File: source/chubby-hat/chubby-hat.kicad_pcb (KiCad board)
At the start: 2 copper layers, 143.5 x 91.4 mm, 148 parts, among them J1 RP2040.SWD, J10 USB_C_Receptacle_USB2.0, J11 HUB75, J12 HUB75, J13 HUB75, J14 v7.0, J15 v8.0, J16 HUB75, J17 Conn_01x02, J18 HUB75, J19 HUB75, J2 Conn_ARM_JTAG_SWD_10, J20 V7.0, J21 V8.0, J22 HUB75, J23 HUB75, J3 Conn_ARM_JTAG_SWD_10, J4 TC2030, J5 UART, J6 5V, J7 5V, J8 5V, J9 5V, Q1 BC807DS,115, Q2 AO3401A, Q3 BC807DS,115, Q4 AO3401A, SW1 RUN, SW2 BOOT, U1 AMS1117-3.3, U2 RP2040-Zero, U3 USBLC6-2SC6, U4 P25Q40H-SSH-IT, U5 RP2040, Y1 12M

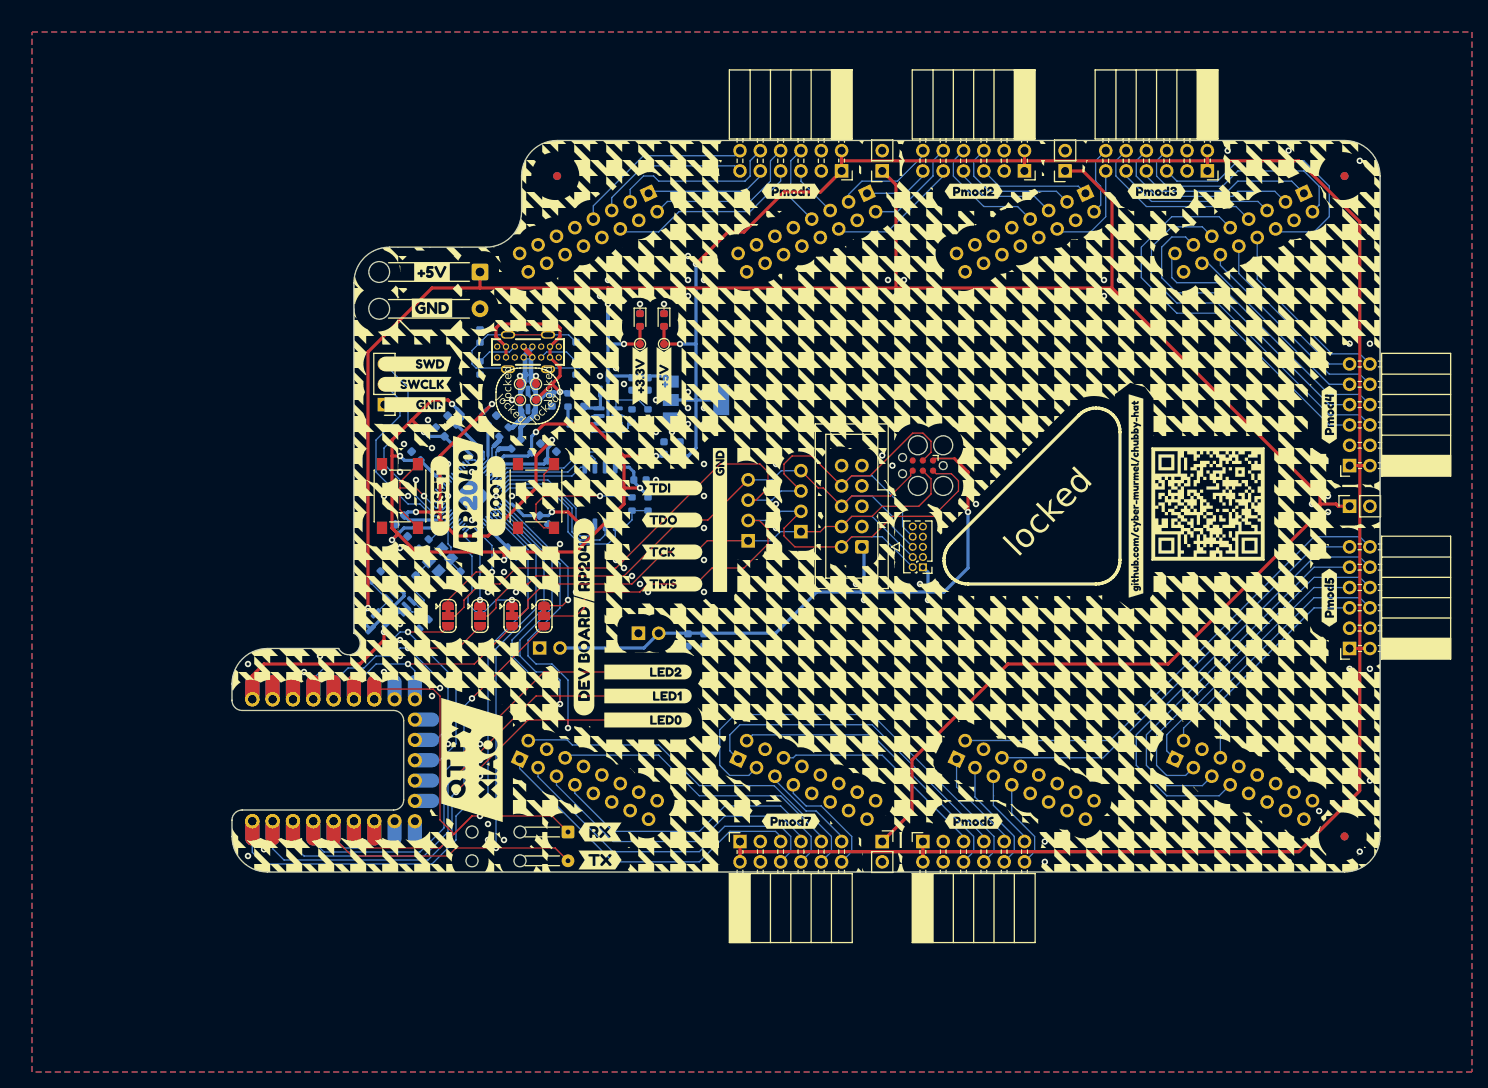
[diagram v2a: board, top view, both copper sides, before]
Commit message: rotated v8 jtag connector - closes #10; moved aux jtag connectors and pmod wires to makes space for #14;
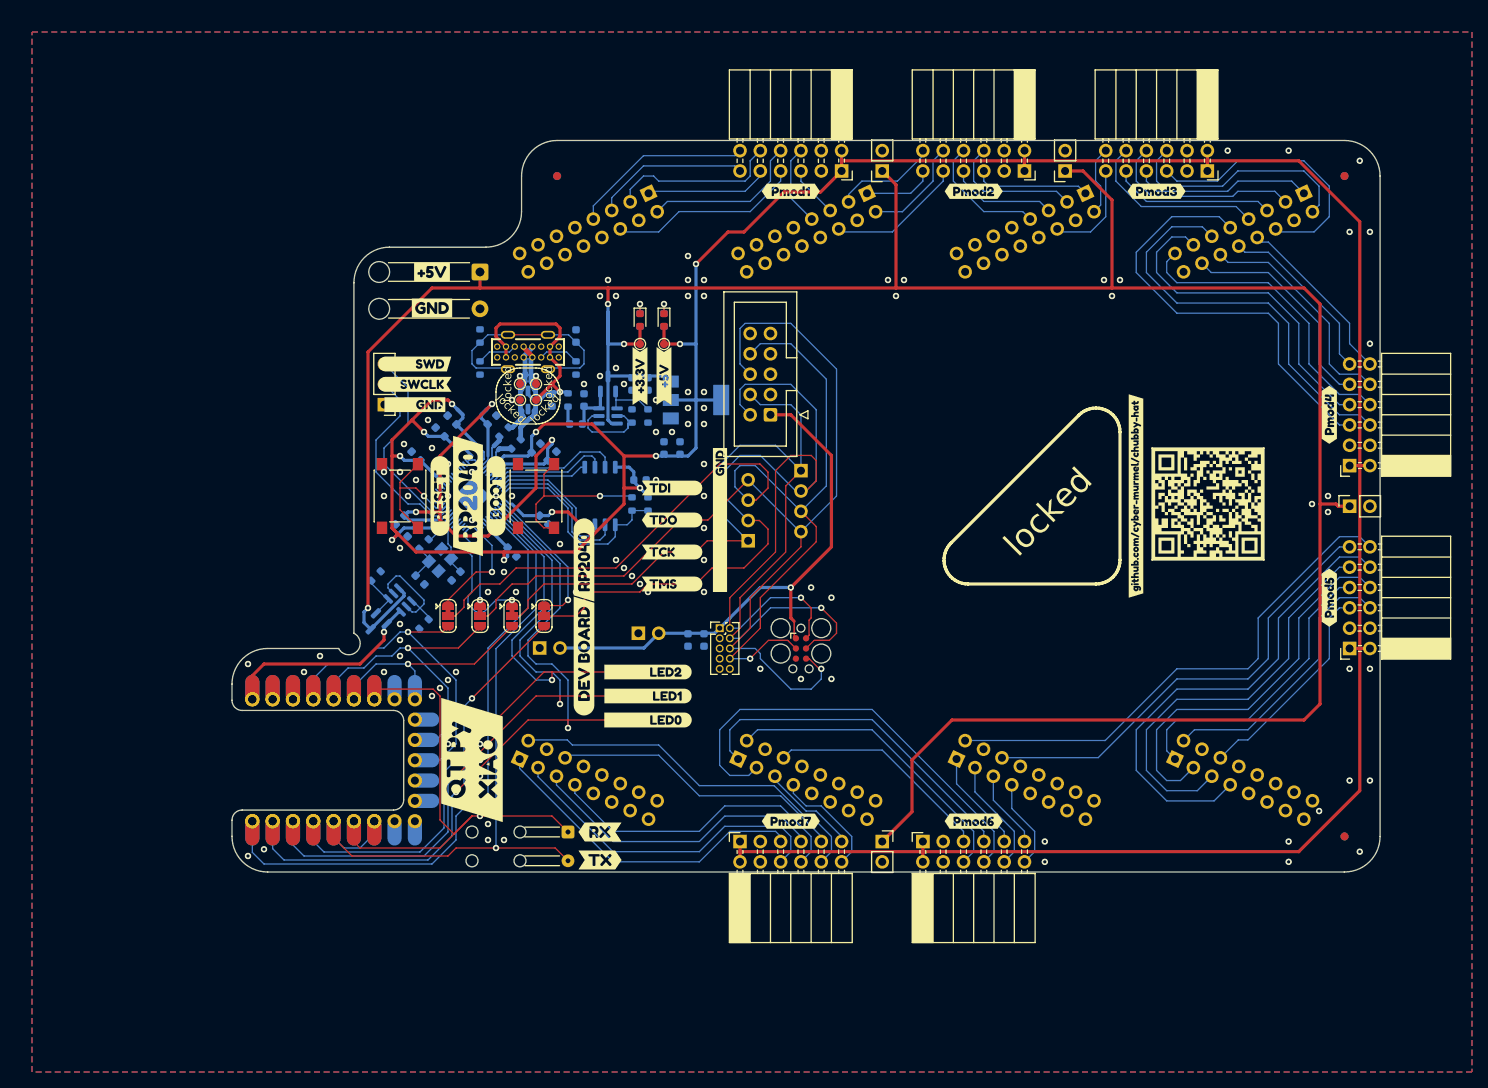
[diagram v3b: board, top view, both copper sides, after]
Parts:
- moved J4 27.5 mm to (198.1, 99.1), turned to -90 degrees
- moved J3 26.5 mm to (188.0, 96.5), turned to 0 degrees
- moved J2 20.1 mm to (194.3, 69.8)
- moved J15 7.62 mm to (198.1, 76.8), turned to 180 degrees
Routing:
- net /JTAG.TDO: track 78.9 -> 130.0 mm, vias 0 -> 1
- net /JTAG.TCK: track 74.1 -> 118.5 mm, vias 0 -> 1
- net /JTAG.TMS: track 89.4 -> 132.3 mm, vias 0 -> 1
- net +5V: track 329.1 -> 357.2 mm
- net /JTAG.TDI: track 105.7 -> 132.2 mm, vias 0 -> 1
- net VDD: track 81.9 -> 66.9 mm
- net /Pmod7_IO2: track 47.6 -> 51.8 mm
- net /Pmod7_IO6: track 56.6 -> 60.9 mm
- net /Pmod7_IO7: track 44.7 -> 48.9 mm
- net /Pmod1_IO7: track 34.5 -> 38.0 mm
- net /Pmod1_IO8: track 47.8 -> 51.3 mm
- net /Pmod1_IO3: track 38.8 -> 42.3 mm
- net /Pmod1_IO4: track 50.7 -> 54.2 mm
- net /Pmod7_IO3: track 33.9 -> 37.3 mm
- net /Pmod7_IO1: track 54.4 -> 57.4 mm
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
